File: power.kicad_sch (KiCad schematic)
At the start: 29 parts, among them CN104 Barrel_Jack, IC109 L7805, SW101 SW_SPDT

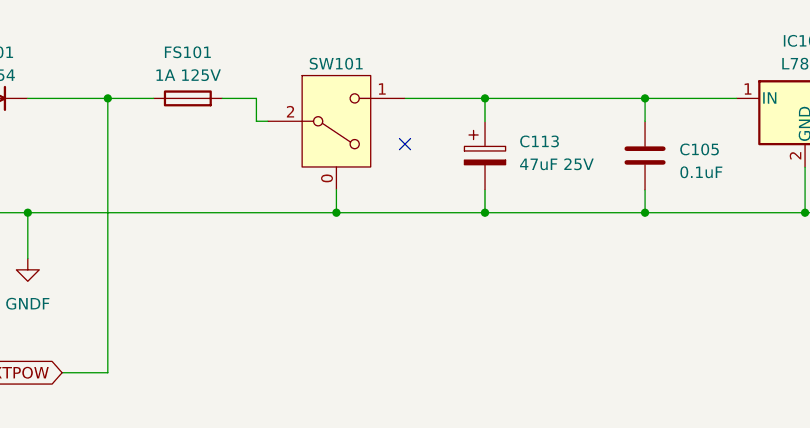
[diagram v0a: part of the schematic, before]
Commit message: Silkscreen fixes
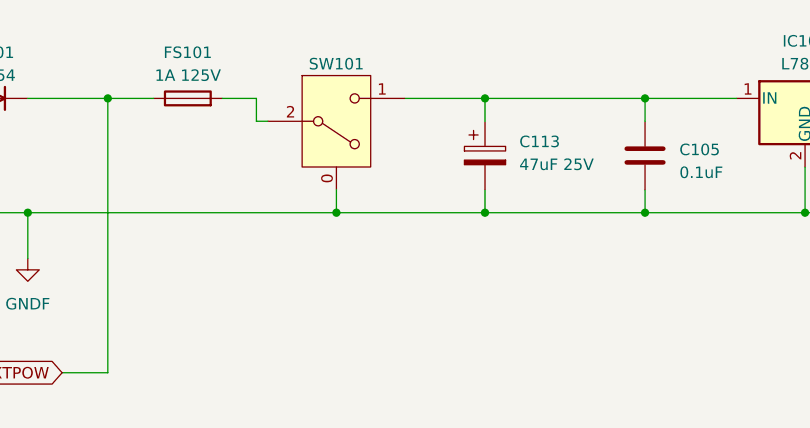
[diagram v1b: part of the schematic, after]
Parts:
- L106: footprint A-PCENGINE:L-5.00mm -> A-PCENGINE:L-5.00mm_Small_Silk
- OSC101: footprint Oscillator:Oscillator_DIP-14 -> A-PCENGINE:Oscillator
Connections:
- no-connect marks 2 -> 1
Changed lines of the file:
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@@
   )
   (no_connect (at 233.68 129.54))
-  (no_connect (at 208.28 55.88))
   (bus_entry (at 118.11 158.75) (size -2.54 2.54)
     (stroke (width 0) (type default))
@@
       (effects (font (size 1.27 1.27)))
     )
-    (property "Footprint" "Oscillator:Oscillator_DIP-14" (at 252.73 138.43 0)
+    (property "Footprint" "A-PCENGINE:Oscillator" (at 252.73 138.43 0)
       (effects (font (size 1.27 1.27)) hide)
     )
@@
       (effects (font (size 1.27 1.27)))
     )
-    (property "Footprint" "A-PCENGINE:L-5.00mm" (at 241.3 109.22 0)
-      (effects (font (size 1.27 1.27)) hide)
-    )
+    (property "Footprint" "A-PCENGINE:L-5.00mm_Small_Silk" (at 241.3 109.22 0)
+      (effects (font (size 1.27 1.27)) hide)
+    )

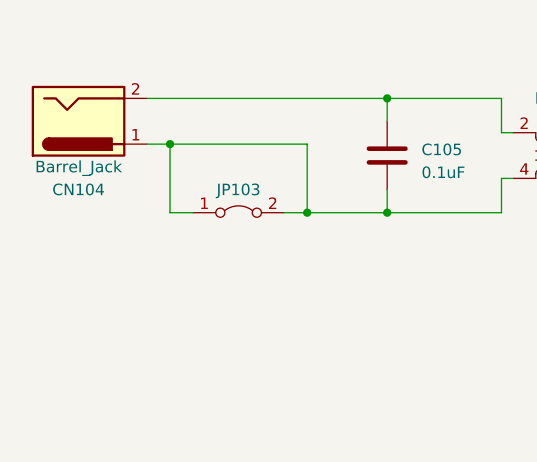
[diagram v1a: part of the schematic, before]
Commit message: Remove some sharp corners on traces, generate BOM.
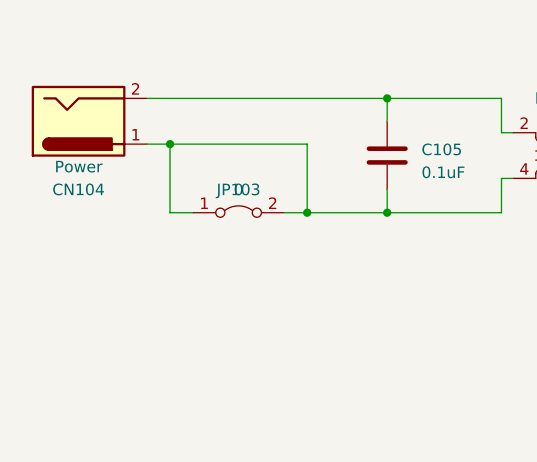
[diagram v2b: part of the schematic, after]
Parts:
- CN104: value Barrel_Jack -> Power
- JP103: value ~ -> 0
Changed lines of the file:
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@@
       (effects (font (size 1.27 1.27)))
     )
-    (property "Value" "~" (at 109.22 60.96 0)
+    (property "Value" "0" (at 109.22 60.96 0)
       (effects (font (size 1.27 1.27)))
     )
@@
       (effects (font (size 1.27 1.27)))
     )
-    (property "Value" "Barrel_Jack" (at 91.44 58.42 0)
-      (effects (font (size 1.27 1.27)))
-    )
+    (property "Value" "Power" (at 91.44 58.42 0)
+      (effects (font (size 1.27 1.27)))
+    )
